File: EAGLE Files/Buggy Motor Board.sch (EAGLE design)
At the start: 41 parts, among them IC1 ILD213T, IC2 ILD213T, IC3 ILD213T, IC4 4050D, IC5 LP298XS, IC6 74LS595D, U1 MCP2551, X1 MICROSD, Y2 16MHZ

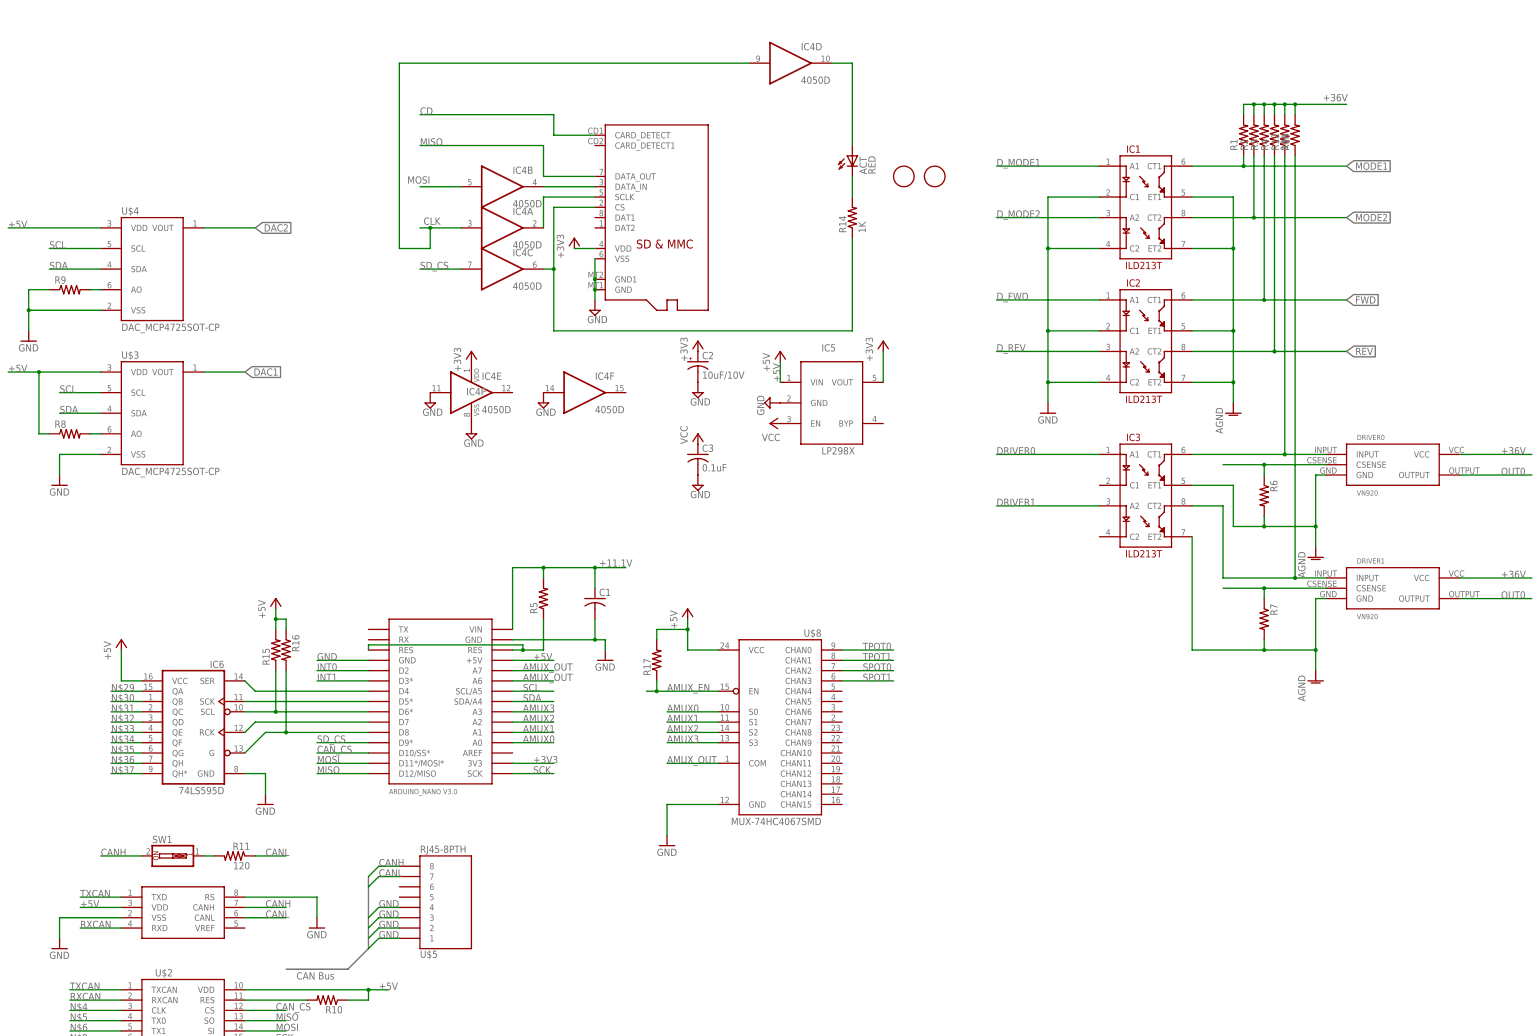
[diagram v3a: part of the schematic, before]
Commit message: Add frame
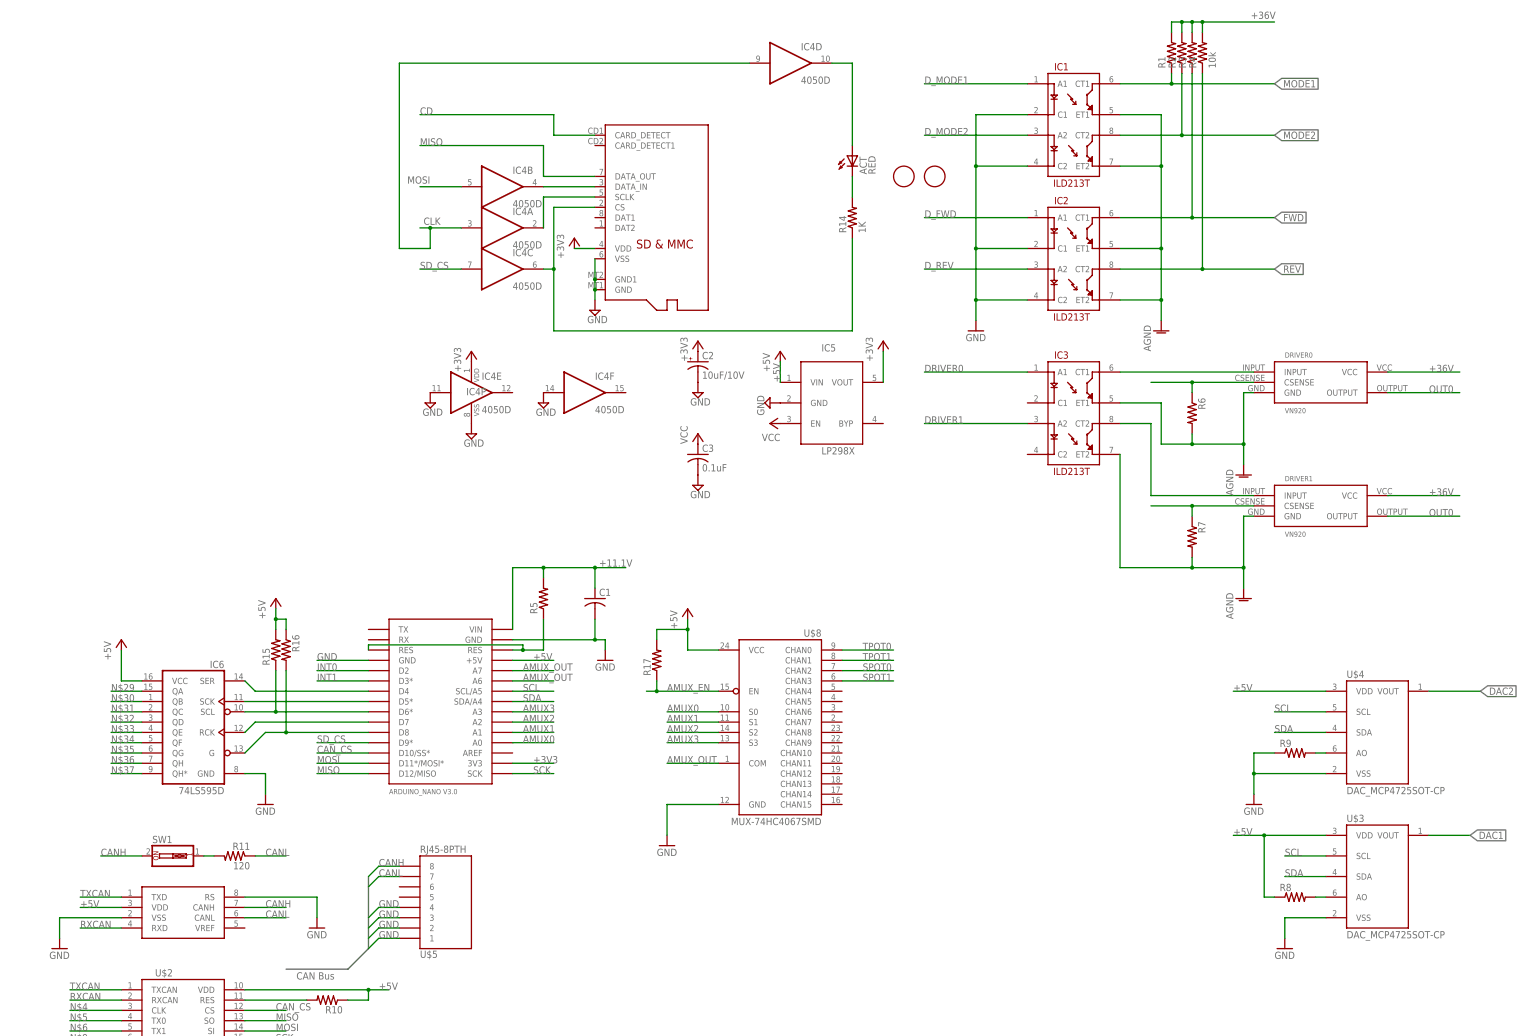
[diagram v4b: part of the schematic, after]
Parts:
- removed R12, R13: (no value), rcl:R-US_R1206
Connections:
- net +36V: no longer R12.2, R13.2
- net N$1: no longer R12.1
- net N$16: no longer R13.1
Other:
- moved on the sheet: DRIVER0, DRIVER1, IC1, IC2, IC3, R1, R2, R3, R4, R6, R7, R8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

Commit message: Optoisolators, MPU9150, cleanup
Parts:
- removed IC1, IC2, IC3: ILD213T, SparkFun-DiscreteSemi:ILD213T
- removed U$6, U$7: FIDUCIAL, adafruit:FIDUCIAL
- added ANALOG_IN: (no value), con-lstb:MA08-2
- added C4, C5, C6, C7: (no value), SparkFun-Capacitors:CAP1206
- added JMP1: 0R-JUMPA, jump-0r-smd:0R-JUMPA
- added OK1, OK2, OK3, OK4: LTV816S, optocoupler:LTV816S
- added R12, R13, R18, R19: 220, adafruit:R-US_R0805
- added R20, R21: 10k, adafruit:R-US_R0805
- added U2: (no value), SparkFun-Sensors:MPU-9150QFN-24-NP
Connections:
- net AMUX_OUT renamed AMUX_IN
- removed net +11.1V: C1.1, R5.2, U$1.VIN
- removed net D_FWD: IC2.A1
- removed net D_MODE1: IC1.A1
- removed net D_MODE2: IC1.A2
- removed net D_REV: IC2.A2
- removed net FWD: IC2.CT1, R3.1
- removed net MODE1: IC1.CT1, R1.1
- removed net MODE2: IC1.CT2, R2.1
- removed net N$32: IC6.QD
- removed net N$33: IC6.QE
- removed net OUT0: DRIVER0.OUTPUT, DRIVER1.OUTPUT
- removed net REV: IC2.CT2, R4.1
- removed net SPOT0: U$8.CHAN2
- removed net SPOT1: U$8.CHAN3
- removed net TPOT0: U$8.CHAN0
- removed net TPOT1: U$8.CHAN1
- new net +12V: C1.1, DRIVER0.VCC, DRIVER1.VCC, R5.2, U$1.VIN
- new net CHAN0: ANALOG_IN.16, U$8.CHAN0
- new net CHAN1: ANALOG_IN.15, U$8.CHAN1
- new net CHAN10: ANALOG_IN.6, U$8.CHAN10
- new net CHAN11: ANALOG_IN.5, U$8.CHAN11
- new net CHAN12: ANALOG_IN.4, U$8.CHAN12
- new net CHAN13: ANALOG_IN.3, U$8.CHAN13
- new net CHAN14: ANALOG_IN.2, U$8.CHAN14
- new net CHAN15: ANALOG_IN.1, U$8.CHAN15
- new net CHAN2: ANALOG_IN.14, U$8.CHAN2
- new net CHAN3: ANALOG_IN.13, U$8.CHAN3
- new net CHAN4: ANALOG_IN.12, U$8.CHAN4
- new net CHAN5: ANALOG_IN.11, U$8.CHAN5
- new net CHAN6: ANALOG_IN.10, U$8.CHAN6
- new net CHAN7: ANALOG_IN.9, U$8.CHAN7
- new net CHAN8: ANALOG_IN.8, U$8.CHAN8
- new net CHAN9: ANALOG_IN.7, U$8.CHAN9
- new net DOUT0: DRIVER0.OUTPUT
- new net DOUT1: DRIVER1.OUTPUT
- new net ESC: U2.E_SCL
- new net ESD: U2.E_SDA
- new net MPUCLKOUT: U2.CLKOUT
- new net N$27: OK3.A, R18.1
- new net OOUT0: OK1.COL, R1.1
- new net OOUT1: OK2.COL, R2.1
- new net OOUT2: OK3.COL, R3.1
- new net OOUT3: OK4.COL, R4.1
- new net OPTO0: IC6.QC, R12.2
- new net OPTO1: IC6.QD, R13.2
- new net OPTO2: IC6.QE, R18.2
- new net OPTO3: IC6.QF, R19.2
- net +36V: no longer DRIVER0.VCC, DRIVER1.VCC
- net +3V3: now also C6.1, C7.1, JMP1-0R.3, R20.2, R21.2, U2.VDD@13, U2.VDD@3, U2.VLOGIC
- net +5V: no longer R17.2
- net AGND: now also OK1.EMIT, OK2.EMIT, OK3.EMIT, OK4.EMIT; no longer DRIVER0.GND, DRIVER1.GND, IC1.ET1, IC1.ET2, IC2.ET1, IC2.ET2, IC3.ET1, IC3.ET2, R6.2, R7.2
- net AMUX_EN: now also R17.2; no longer R17.1
- net DRIVER0: now also DRIVER0.INPUT, IC6.QA; no longer IC3.A1
- net DRIVER1: now also DRIVER1.INPUT, IC6.QB; no longer IC3.A2
- net GND: now also C4.2, C5.2, C6.2, C7.2, DRIVER0.GND, DRIVER1.GND, JMP1-0R.1, OK1.C, OK2.C, OK3.C, OK4.C, R17.1, R6.1, R7.1, U2.CLKIN, U2.FSYNC, U2.GND@15, U2.GND@17, U2.GND@18; no longer IC1.C1, IC1.C2, IC2.C1, IC2.C2
- net INT1: now also U2.INT
- net N$1: now also DRIVER0.CSENSE, R6.2; no longer DRIVER0.INPUT, IC3.CT1
- net N$12: now also OK1.A, R12.1; no longer DRIVER0.CSENSE, R6.1
- net N$15: now also OK2.A, R13.1; no longer DRIVER1.CSENSE, R7.1
- net N$16: now also DRIVER1.CSENSE, R7.2; no longer DRIVER1.INPUT, IC3.CT2
- net N$29: now also OK4.A, R19.1; no longer IC6.QA
- net N$30: now also C4.1, U2.REGOUT; no longer IC6.QB
- net N$31: now also C5.1, U2.CPOUT; no longer IC6.QC
- net N$34: now also JMP1-0R.2, U2.AD0; no longer IC6.QF
- net SCL: now also R21.1, U2.SCL
- net SDA: now also R20.1, U2.SDA
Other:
- moved on the sheet: ACT, C2, C3, DRIVER0, DRIVER1, IC4A, IC4B, IC4C, IC4D, IC4E, IC4F, IC4P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

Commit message: Second shift register
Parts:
- added C8: (no value), rcl:C-USC1210K
- added IC1: 74LS595D, SparkFun-DigitalIC:74LS595D
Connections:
- new net N$32: IC1.SER, IC6.QH*
- new net N$36: IC1.QC
- new net N$38: IC1.QE
- new net N$39: IC1.QF
- new net N$40: IC1.QG
- new net N$41: IC1.QH
- net CAN_CS: now also IC1.QB; no longer U$1.D10/SS*
- net GND: now also C8.2, IC1.GND
- net N$22: now also IC1.SCL
- net N$25: now also IC1.SCK
- net N$26: now also C8.1, IC1.RCK
- net N$28: now also IC1.G
- net N$37: now also IC1.QD; no longer IC6.QH*
- net SD_CS: now also IC1.QA; no longer U$1.D9*
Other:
- moved on the sheet: C1, IC6, R10, R11, R15, R16, R5, SW1, U$2, U$5, Y2

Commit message: Second optocoupler
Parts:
- removed OK2, OK3, OK4: LTV816S, optocoupler:LTV816S
- added OK5: TIL199, optocoupler:TIL199
- added R22, R23, R24, R25: 220, adafruit:R-US_R0805
- added R26, R27, R28: (no value), rcl:R-US_R1206
- added R29: 10k, rcl:R-US_R1206
- OK1: value LTV816S -> TIL199; device optocoupler:LTV816S -> optocoupler:TIL199
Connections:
- removed net N$35: IC6.QH
- new net N$42: OK1C.A, R24.1
- new net OOUT4: OK1A.COL, R26.1
- new net OOUT5: OK1B.COL, R27.1
- new net OOUT6: OK1C.COL, R28.1
- new net OOUT7: OK1D.COL, R29.1
- new net OPTO4: IC6.QE, R22.2
- new net OPTO5: IC6.QF, R23.2
- new net OPTO6: IC6.QG, R24.2
- new net OPTO7: IC6.QH, R25.2
- net +36V: now also R26.2, R27.2, R28.2, R29.2
- net AGND: now also OK5A.EMI, OK5B.EMI, OK5C.EMI, OK5D.EMI; no longer OK1.EMIT, OK2.EMIT, OK3.EMIT, OK4.EMIT
- net DRIVER0: now also IC1.QC; no longer IC6.QA
- net DRIVER1: now also IC1.QD; no longer IC6.QB
- net GND: now also OK5A.C, OK5B.C, OK5C.C, OK5D.C; no longer OK1.C, OK2.C, OK3.C, OK4.C
- net N$12: now also OK5A.A; no longer OK1.A
- net N$15: now also OK5B.A; no longer OK2.A
- net N$27: now also OK5C.A; no longer OK3.A
- net N$29: now also OK5D.A; no longer OK4.A
- net N$33: now also OK1D.A, R25.1; no longer IC6.QG
- net N$36: now also OK1A.A, R22.1; no longer IC1.QC
- net N$37: now also OK1B.A, R23.1; no longer IC1.QD
- net OOUT0: now also OK5A.COL; no longer OK1.COL
- net OOUT1: now also OK5B.COL; no longer OK2.COL
- net OOUT2: now also OK5C.COL; no longer OK3.COL
- net OOUT3: now also OK5D.COL; no longer OK4.COL
- net OPTO0: now also IC6.QA; no longer IC6.QC
- net OPTO1: now also IC6.QB; no longer IC6.QD
- net OPTO2: now also IC6.QC; no longer IC6.QE
- net OPTO3: now also IC6.QD; no longer IC6.QF
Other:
- moved on the sheet: ACT, C1, C2, C3, C4, C5, C6, C7, C8, IC1, IC4A, IC4B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

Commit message: Add molex connectors for curtis controllers
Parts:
- added X2, X3: 5566-6, con-molex:5566-6
- added X4, X5: 5566-24, con-molex:5566-24
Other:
- note added: "A"
- note added: "For UNCA Motorsports 2015-2016"
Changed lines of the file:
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@@
 <part name="R28" library="rcl" deviceset="R-US_" device="R1206"/>
 <part name="R29" library="rcl" deviceset="R-US_" device="R1206" value="10k"/>
+<part name="X2" library="con-molex" deviceset="5566-6" device=""/>
+<part name="X3" library="con-molex" deviceset="5566-6" device=""/>
+<part name="X4" library="con-molex" deviceset="5566-24" device=""/>
+<part name="X5" library="con-molex" deviceset="5566-24" device=""/>
 </parts>
 <sheets>
@@
 <plain>
 <text x="243.84" y="53.34" size="1.778" layer="95">CAN Bus</text>
+<text x="200.66" y="-63.5" size="1.778" layer="94">For UNCA Motorsports 2015-2016</text>
+<text x="285.496" y="-85.09" size="3.81" layer="94" ratio="10">A</text>
 </plain>
 <instances>
@@
 <instance part="R28" gate="G$1" x="-35.56" y="121.92" rot="R90"/>
 <instance part="R29" gate="G$1" x="-33.02" y="121.92" rot="R90"/>
+<instance part="X2" gate="-1" x="-88.9" y="177.8"/>
+<instance part="X2" gate="-2" x="-88.9" y="175.26"/>
+<instance part="X2" gate="-3" x="-88.9" y="172.72"/>
+<instance part="X2" gate="-4" x="-88.9" y="170.18"/>
+<instance part="X2" gate="-5" x="-88.9" y="167.64"/>
+<instance part="X2" gate="-6" x="-88.9" y="165.1"/>
+<instance part="X3" gate="-1" x="-88.9" y="160.02"/>
+<instance part="X3" gate="-2" x="-88.9" y="157.48"/>
+<instance part="X3" gate="-3" x="-88.9" y="154.94"/>
+<instance part="X3" gate="-4" x="-88.9" y="152.4"/>
+<instance part="X3" gate="-5" x="-88.9" y="149.86"/>
+<instance part="X3" gate="-6" x="-88.9" y="147.32"/>
+<instance part="X4" gate="-1" x="25.4" y="177.8"/>
+<instance part="X4" gate="-2" x="25.4" y="175.26"/>
+<instance part="X4" gate="-3" x="25.4" y="172.72"/>
+<instance part="X4" gate="-4" x="25.4" y="170.18"/>
+<instance part="X4" gate="-5" x="25.4" y="167.64"/>
+<instance part="X4" gate="-6" x="25.4" y="165.1"/>
+<instance part="X4" gate="-7" x="25.4" y="162.56"/>
+<instance part="X4" gate="-8" x="25.4" y="160.02"/>
+<instance part="X4" gate="-9" x="25.4" y="157.48"/>
+<instance part="X4" gate="-10" x="25.4" y="154.94"/>
+<instance part="X4" gate="-11" x="25.4" y="152.4"/>
+<instance part="X4" gate="-12" x="25.4" y="149.86"/>
+<instance part="X4" gate="-13" x="25.4" y="147.32"/>
+<instance part="X4" gate="-14" x="25.4" y="144.78"/>
+<instance part="X4" gate="-15" x="25.4" y="142.24"/>
+<instance part="X4" gate="-16" x="25.4" y="139.7"/>
+<instance part="X4" gate="-17" x="25.4" y="137.16"/>
+<instance part="X4" gate="-18" x="25.4" y="134.62"/>
+<instance part="X4" gate="-19" x="25.4" y="132.08"/>
+<instance part="X4" gate="-20" x="25.4" y="129.54"/>
+<instance part="X4" gate="-21" x="25.4" y="127"/>
+<instance part="X4" gate="-22" x="25.4" y="124.46"/>
+<instance part="X4" gate="-23" x="25.4" y="121.92"/>
+<instance part="X4" gate="-24" x="25.4" y="119.38"/>
+<instance part="X5" gate="-1" x="25.4" y="114.3"/>
+<instance part="X5" gate="-2" x="25.4" y="111.76"/>
+<instance part="X5" gate="-3" x="25.4" y="109.22"/>
+<instance part="X5" gate="-4" x="25.4" y="106.68"/>
+<instance part="X5" gate="-5" x="25.4" y="104.14"/>
+<instance part="X5" gate="-6" x="25.4" y="101.6"/>
+<instance part="X5" gate="-7" x="25.4" y="99.06"/>
+<instance part="X5" gate="-8" x="25.4" y="96.52"/>
+<instance part="X5" gate="-9" x="25.4" y="93.98"/>
+<instance part="X5" gate="-10" x="25.4" y="91.44"/>
+<instance part="X5" gate="-11" x="25.4" y="88.9"/>
+<instance part="X5" gate="-12" x="25.4" y="86.36"/>
+<instance part="X5" gate="-13" x="25.4" y="83.82"/>
+<instance part="X5" gate="-14" x="25.4" y="81.28"/>
+<instance part="X5" gate="-15" x="25.4" y="78.74"/>
+<instance part="X5" gate="-16" x="25.4" y="76.2"/>
+<instance part="X5" gate="-17" x="25.4" y="73.66"/>
+<instance part="X5" gate="-18" x="25.4" y="71.12"/>
+<instance part="X5" gate="-19" x="25.4" y="68.58"/>
+<instance part="X5" gate="-20" x="25.4" y="66.04"/>
+<instance part="X5" gate="-21" x="25.4" y="63.5"/>
+<instance part="X5" gate="-22" x="25.4" y="60.96"/>
+<instance part="X5" gate="-23" x="25.4" y="58.42"/>
+<instance part="X5" gate="-24" x="25.4" y="55.88"/>
 </instances>
 <busses>
